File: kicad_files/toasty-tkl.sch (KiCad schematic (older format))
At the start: 204 parts, among them CON1 USB-MINI-B, Q1 FET_N, SW0:0 ESC, SW0:10 F9, SW0:11 F10, SW0:12 F11, SW0:13 F12, SW0:14 PRINT, SW0:15 SCROLL LOCK, SW0:2 F1, SW0:3 F2, SW0:4 F3, SW0:5 F4, SW0:6 F5, SW0:7 F6, SW0:8 F7, SW0:9 F8, SW1:0 `, SW1:1 1, SW1:10 0, SW1:11 -, SW1:12 =, SW1:13 BACK SPACE, SW1:14 INSERT, SW1:15 HOME, SW1:2 2, SW1:3 3, SW1:4 4, SW1:5 5, SW1:6 6, SW1:7 7, SW1:8 8, SW1:9 9, SW2:0 TAB, SW2:1 Q, SW2:10 P, SW2:11 [, SW2:12 ], SW2:13 \\, SW2:14 DELETE, SW2:15 END, SW2:2 W, SW2:3 E, SW2:4 R, SW2:5 T, SW2:6 Y, SW2:7 U, SW2:8 I, SW2:9 O, SW3:0 CAPS LOCK, SW3:1 A, SW3:10 ;, SW3:11 ', SW3:13 ENTER, SW3:14 PAGE UP, SW3:15 PAUSE, SW3:2 S, SW3:3 D, SW3:4 F, SW3:5 G, SW3:6 H, SW3:7 J, SW3:8 K, SW3:9 L, SW4:0 LEFT SHIFT, SW4:1 Z, SW4:10 /, SW4:13 RIGHT SHIFT, SW4:14 PAGE DOWN, SW4:15 UP, SW4:2 X, SW4:3 C, SW4:4 V, SW4:5 B, SW4:6 N, SW4:7 M, SW4:8 ,, SW4:9 ., SW5:0 LEFT CTRL, SW5:1 LEFT WINDOWS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

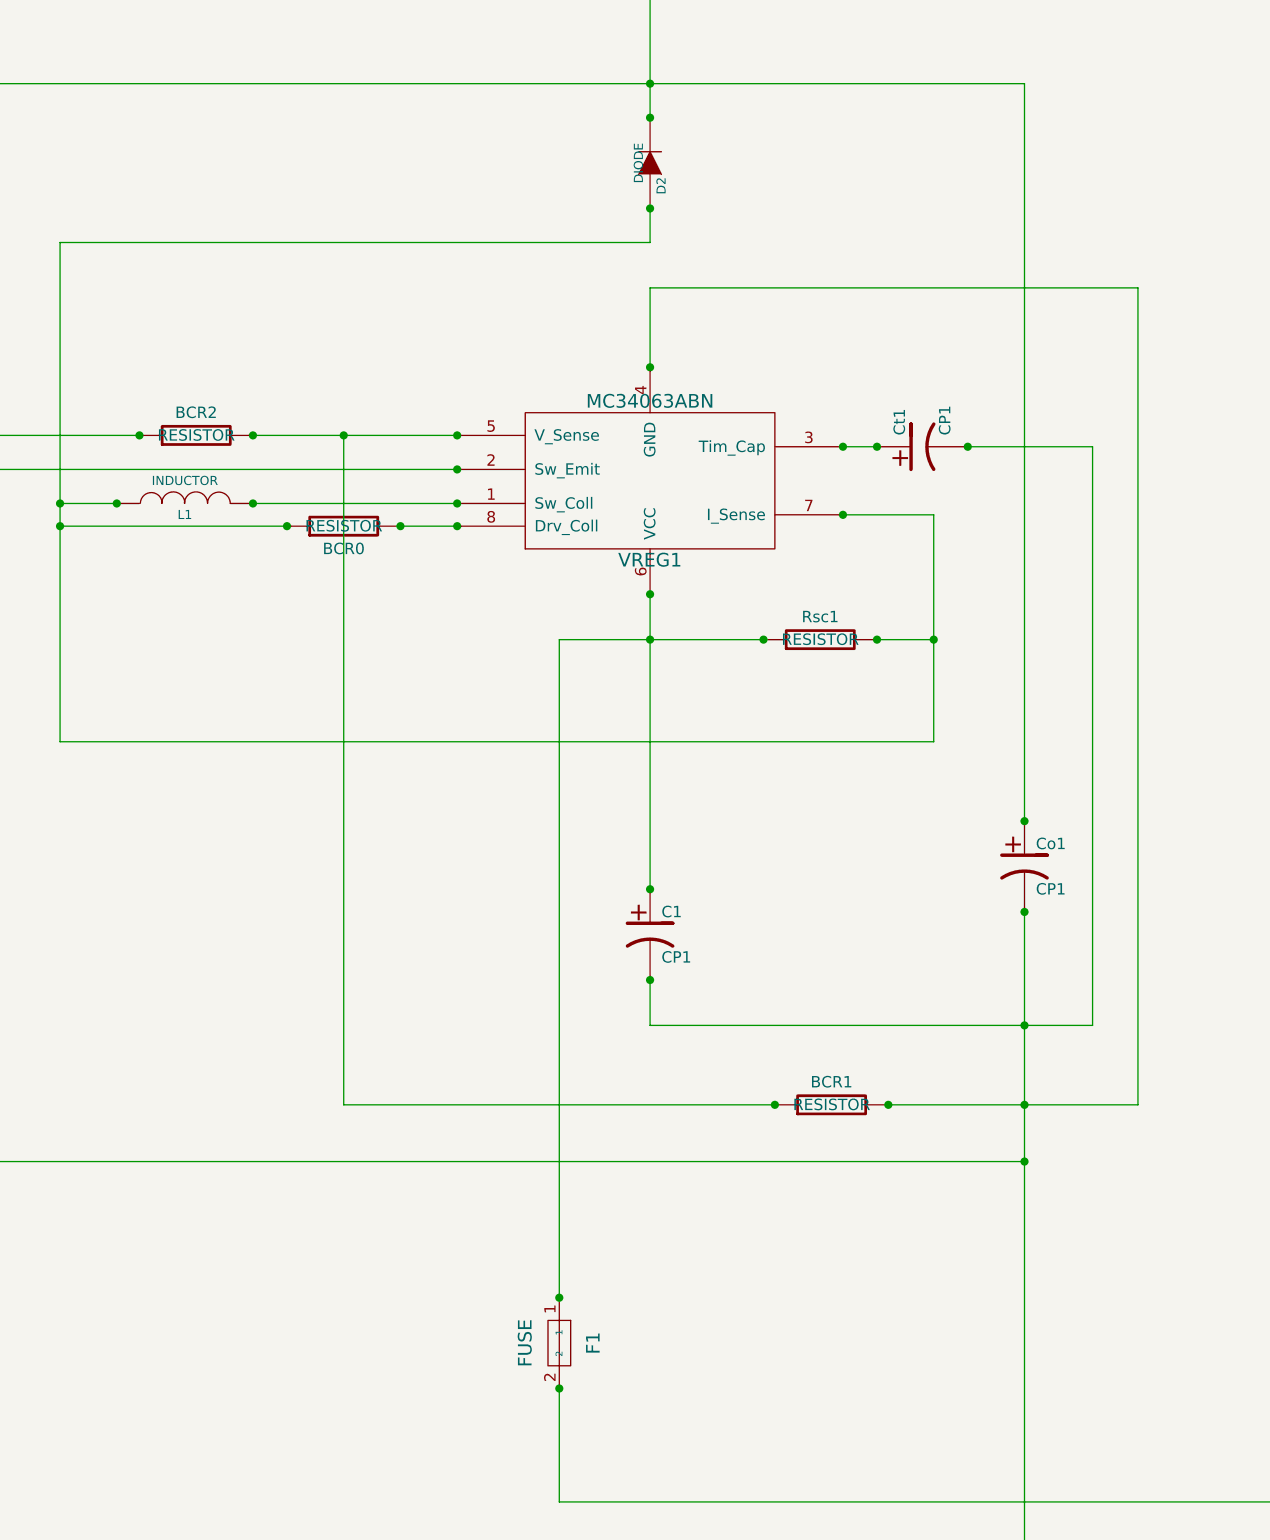
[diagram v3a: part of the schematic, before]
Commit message: Fixed up my footprints, added into kicad diag.
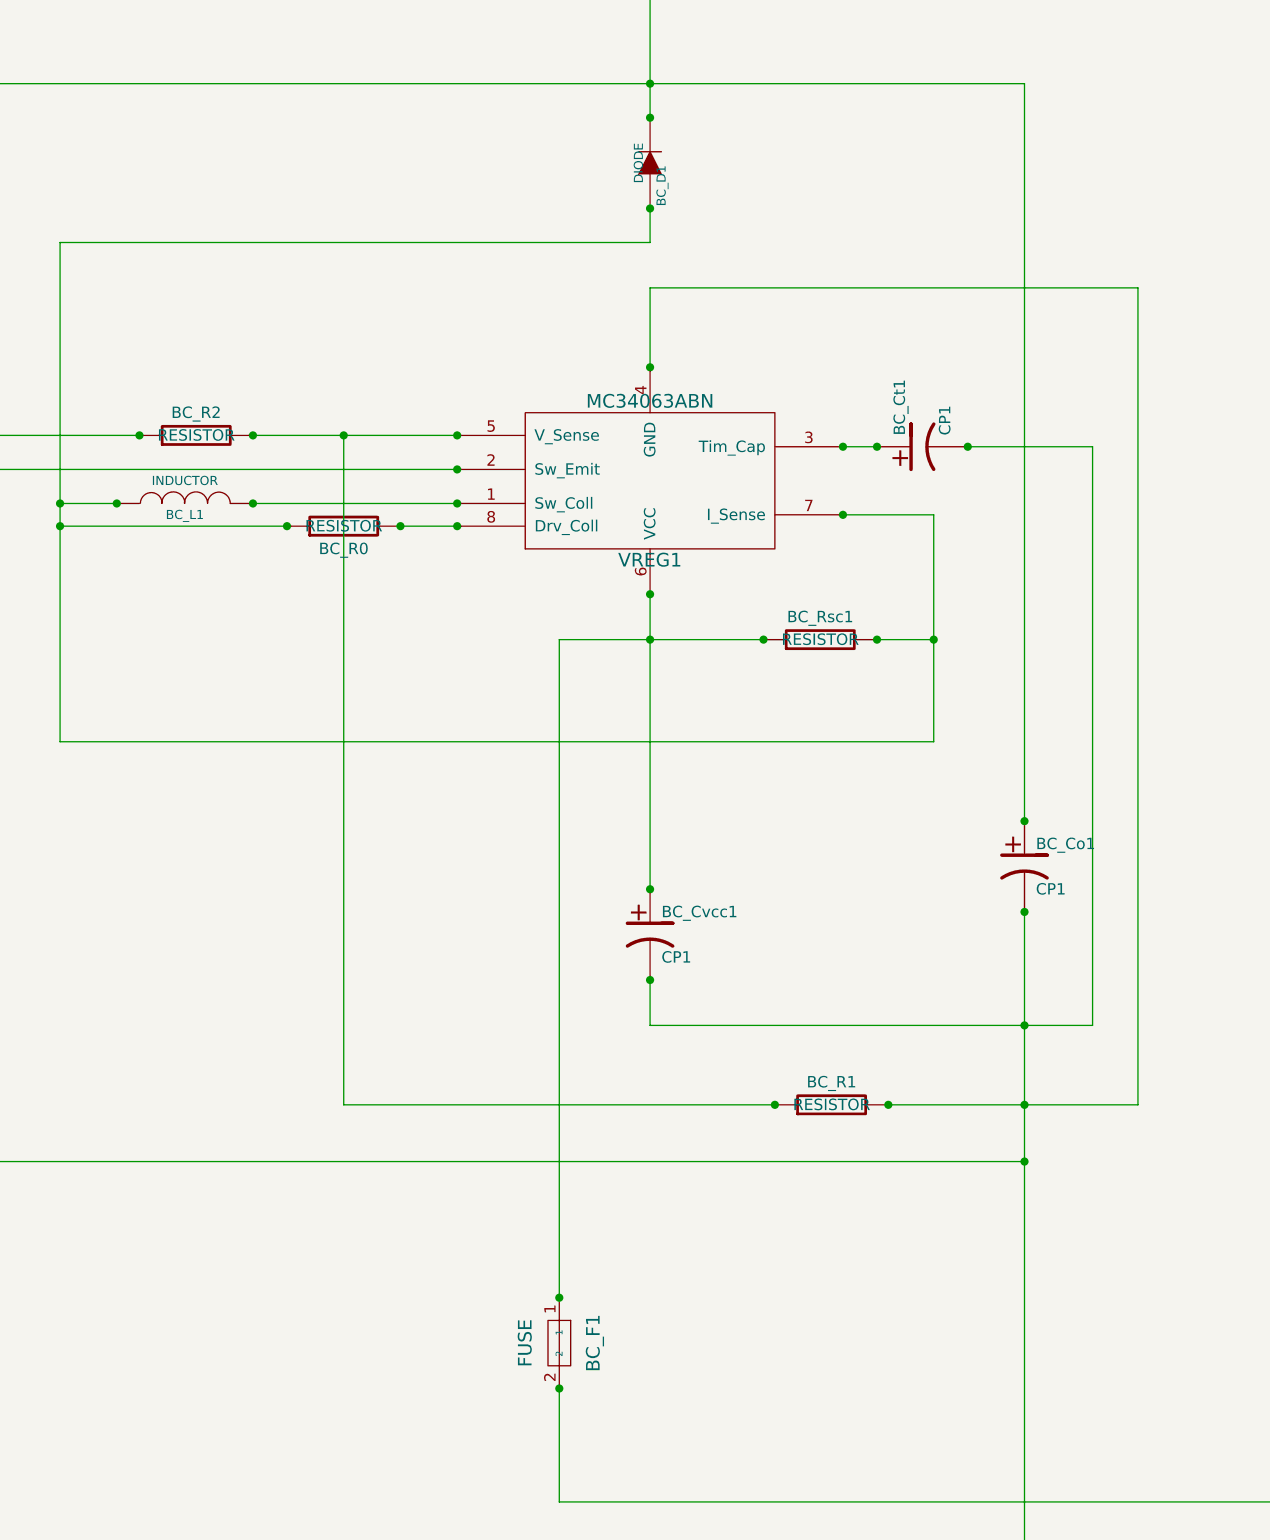
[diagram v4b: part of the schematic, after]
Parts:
- renumbered Co1 to BC_Co1, Ct1 to BC_Ct1, C1 to BC_Cvcc1, D2 to BC_D1, F1 to BC_F1, L1 to BC_L1, BCR0 to BC_R0, BCR1 to BC_R1, BCR2 to BC_R2, Rsc1 to BC_Rsc1
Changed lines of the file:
@@
-EESchema Schematic File Version 2  date 23/06/2013 4:53:48 PM
+EESchema Schematic File Version 2
 LIBS:components
 LIBS:toasty-tkl-cache
@@
 Sheet 1 1
 Title "Toasty TKL"
-Date "23 jun 2013"
+Date "24 jun 2013"
 Rev "REV 1A"
 Comp ""
@@
 $EndComp
 $Comp
-L FUSE F1
+L FUSE BC_F1
 U 1 1 519CE3F5
 P -2050 12600
-F 0 "F1" H -2050 12450 60  0000 C CNN
+F 0 "BC_F1" H -2050 12450 60  0000 C CNN
 F 1 "FUSE" H -2050 12750 60  0000 C CNN
 F 2 "" H -2050 12600 60  0000 C CNN
@@
 $EndComp
 $Comp
-L CP1 C1
+L CP1 BC_Cvcc1
 U 1 1 51BE5B31
 P -1650 10800
-F 0 "C1" H -1600 10900 50  0000 L CNN
+F 0 "BC_Cvcc1" H -1600 10900 50  0000 L CNN
 F 1 "CP1" H -1600 10700 50  0000 L CNN
 F 2 "~" H -1650 10800 60  0000 C CNN
@@
 $EndComp
 $Comp
-L CP1 Ct1
+L CP1 BC_Ct1
 U 1 1 51BE5B40
 P -450 8650
-F 0 "Ct1" H -400 8750 50  0000 L CNN
+F 0 "BC_Ct1" H -400 8750 50  0000 L CNN
 F 1 "CP1" H -400 8550 50  0000 L CNN
 F 2 "~" H -450 8650 60  0000 C CNN
@@
 $EndComp
 $Comp
-L RESISTOR BCR0
+L RESISTOR BC_R0
 U 1 1 51BE5B4F
 P -3000 9000
-F 0 "BCR0" V -3100 9000 50  0000 C CNN
+F 0 "BC_R0" V -3100 9000 50  0000 C CNN
 F 1 "RESISTOR" V -3000 9000 50  0000 C CNN
 F 2 "~" H -3000 9000 60  0000 C CNN
@@
 $EndComp
 $Comp
-L RESISTOR Rsc1
+L RESISTOR BC_Rsc1
 U 1 1 51BE5B5E
 P -900 9500
-F 0 "Rsc1" V -800 9500 50  0000 C CNN
+F 0 "BC_Rsc1" V -800 9500 50  0000 C CNN
 F 1 "RESISTOR" V -900 9500 50  0000 C CNN
 F 2 "~" H -900 9500 60  0000 C CNN
@@
 $EndComp
 $Comp
-L RESISTOR BCR2
+L RESISTOR BC_R2
 U 1 1 51BE5B6D
 P -3650 8600
-F 0 "BCR2" V -3550 8600 50  0000 C CNN
+F 0 "BC_R2" V -3550 8600 50  0000 C CNN
 F 1 "RESISTOR" V -3650 8600 50  0000 C CNN
 F 2 "~" H -3650 8600 60  0000 C CNN
@@
 $EndComp
 $Comp
-L RESISTOR BCR1
+L RESISTOR BC_R1
 U 1 1 51BE5B7C
 P -850 11550
-F 0 "BCR1" V -750 11550 50  0000 C CNN
+F 0 "BC_R1" V -750 11550 50  0000 C CNN
 F 1 "RESISTOR" V -850 11550 50  0000 C CNN
 F 2 "~" H -850 11550 60  0000 C CNN
@@
 $EndComp
 $Comp
-L INDUCTOR L1
+L INDUCTOR BC_L1
 U 1 1 51BE5B8B
 P -3700 8900
-F 0 "L1" V -3750 8900 40  0000 C CNN
+F 0 "BC_L1" V -3750 8900 40  0000 C CNN
 F 1 "INDUCTOR" V -3600 8900 40  0000 C CNN
 F 2 "~" H -3700 8900 60  0000 C CNN
@@
 $EndComp
 $Comp
-L DIODE D2
+L DIODE BC_D1
 U 1 1 51BE5B9A
 P -1650 7400
-F 0 "D2" H -1750 7350 40  0000 C CNN
+F 0 "BC_D1" H -1750 7350 40  0000 C CNN
 F 1 "DIODE" H -1650 7450 40  0000 C CNN
 F 2 "~" H -1650 7400 60  0000 C CNN
@@
 $EndComp
 $Comp
-L CP1 Co1
+L CP1 BC_Co1
 U 1 1 51C3F6C2
 P 0 10500
-F 0 "Co1" H 50  10600 50  0000 L CNN
+F 0 "BC_Co1" H 50  10600 50  0000 L CNN
 F 1 "CP1" H 50  10400 50  0000 L CNN
 F 2 "~" H 0   10500 60  0000 C CNN

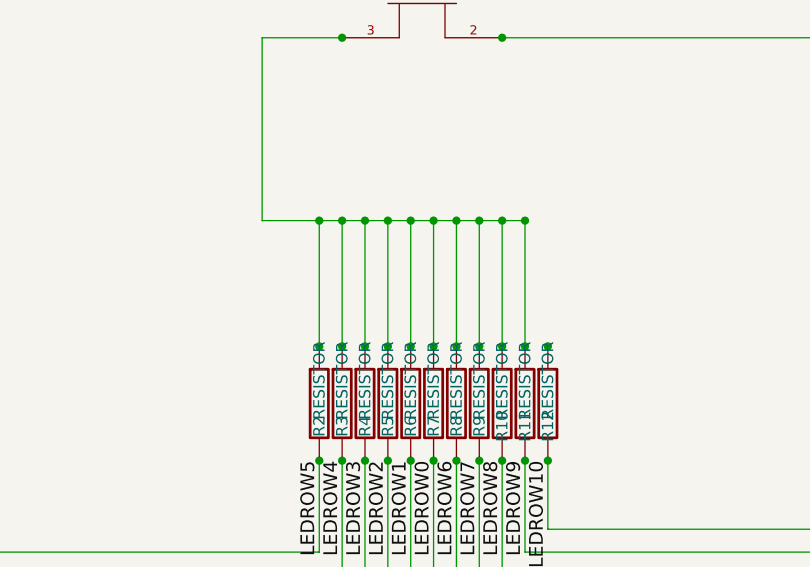
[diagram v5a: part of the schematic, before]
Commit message: Thickened all 10 mil vcc and gnd traces to 20mm and reogranised.
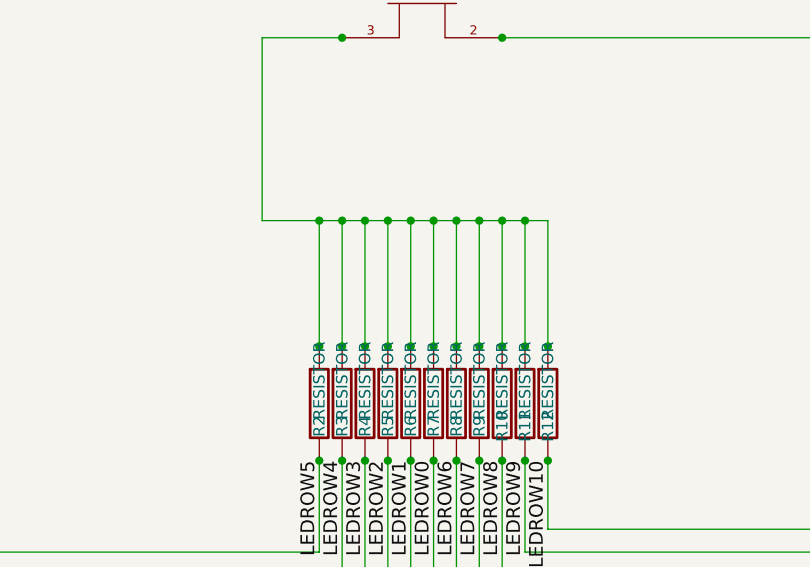
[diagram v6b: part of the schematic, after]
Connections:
- net at Q1.3 (D), R10.1, R11.1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: now also R12.1
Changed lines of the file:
@@
-EESchema Schematic File Version 2  date 25/06/2013 8:46:32 PM
+EESchema Schematic File Version 2
 LIBS:components
 LIBS:toasty-tkl-cache
@@
 Sheet 1 1
 Title "Toasty TKL"
-Date "24 jun 2013"
+Date "27 jun 2013"
 Rev "REV 1A"
 Comp ""
@@
 Connection ~ -800 8650
 Wire Wire Line
-	10300 -2350 9150 -2350
+	9150 -2350 10400 -2350
 Wire Wire Line
 	9150 -2350 9150 -3150
@@
 Connection ~ -2050 12800
 Connection ~ -650 8650
+Wire Wire Line
+	10400 -2350 10400 -1800
 $EndSCHEMATC
